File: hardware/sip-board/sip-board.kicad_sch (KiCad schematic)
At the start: 16 parts, among them Q5 BS170F

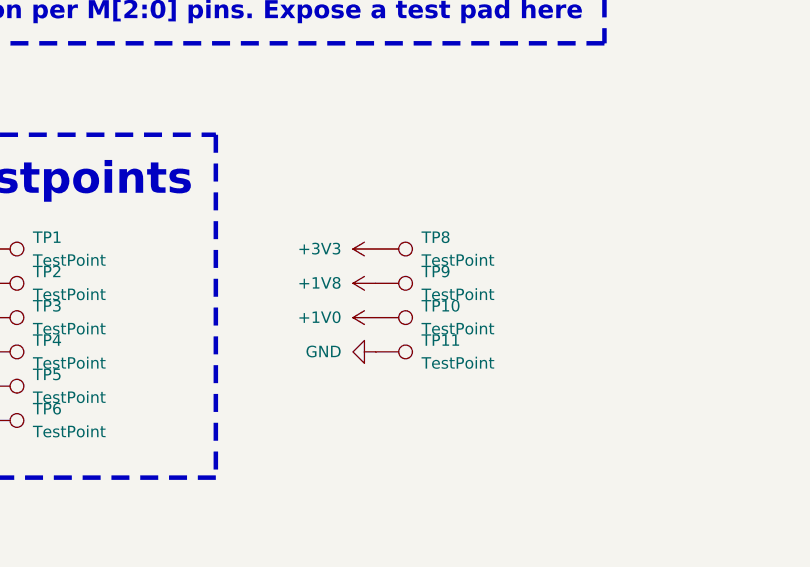
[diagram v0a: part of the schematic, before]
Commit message: sip vreg redo, connect level shifters to outside pins
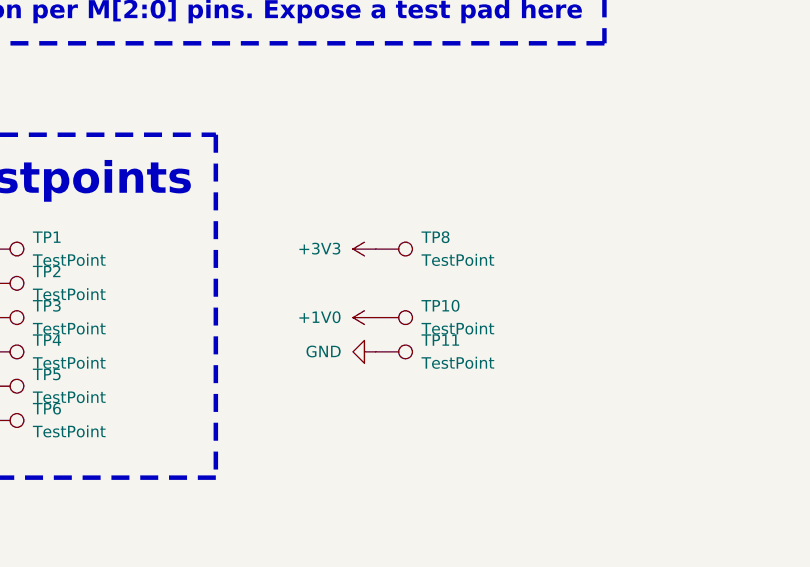
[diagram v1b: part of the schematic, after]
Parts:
- removed TP9: TestPoint, TestPoint:TestPoint_Pad_1.0x1.0mm, symbol Connector:TestPoint
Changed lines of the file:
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@@
-	(symbol
-		(lib_id "Connector:TestPoint")
-		(at 185.42 124.46 270)
-		(unit 1)
-		(exclude_from_sim no)
-		(in_bom yes)
-		(on_board yes)
-		(dnp no)
-		(fields_autoplaced yes)
-		(property "Reference" "TP9"
-			(at 190.5 123.1899 90)
-			(effects
-				(font
-					(size 1.27 1.27)
-				)
-				(justify left)
-			)
-		)
-		(property "Value" "TestPoint"
-			(at 190.5 125.7299 90)
-			(effects
-				(font
-					(size 1.27 1.27)
-				)
-				(justify left)
-			)
-		)
-		(property "Footprint" "TestPoint:TestPoint_Pad_1.0x1.0mm"
-			(at 185.42 129.54 0)
-			(effects
-				(font
-					(size 1.27 1.27)
-				)
-				(hide yes)
-			)
-		)
-		(property "Datasheet" "~"
-			(at 185.42 129.54 0)
-			(effects
-				(font
-					(size 1.27 1.27)
-				)
-				(hide yes)
-			)
-		)
-		(property "Description" "test point"
-			(at 185.42 124.46 0)
-			(effects
-				(font
-					(size 1.27 1.27)
-				)
-				(hide yes)
-			)
-		)
-		(pin "1"
-		)
-		(instances
-			(project "sip-board"
-				(path "/4eae758a-da4d-4448-84d4-770db7217b0d"
-					(reference "TP9")
-					(unit 1)
-				)
-			)
-		)
-	)
 	(symbol
 		(lib_id "Connector:TestPoint")
@@
 					(unit 1)
 				)
-			)
-		)
-	)
-	(symbol
-		(lib_id "power:+1V8")
-		(at 185.42 124.46 90)
-		(unit 1)
-		(exclude_from_sim no)
-		(in_bom yes)
-		(on_board yes)
-		(dnp no)
-		(fields_autoplaced yes)
-		(property "Reference" "#PWR0145"
-			(at 189.23 124.46 0)
-			(effects
-				(font
-					(size 1.27 1.27)
-				)
-				(hide yes)
-			)
-		)
-		(property "Value" "+1V8"
-			(at 181.61 124.4599 90)
-			(effects
-				(font
-					(size 1.27 1.27)
-				)
-				(justify left)
-			)
-		)
-		(property "Footprint" ""
-			(at 185.42 124.46 0)
-			(effects
-				(font
-					(size 1.27 1.27)
-				)
-				(hide yes)
-			)
-		)
-		(property "Datasheet" ""
-			(at 185.42 124.46 0)
-			(effects
-				(font
-					(size 1.27 1.27)
-				)
-				(hide yes)
-			)
-		)
-		(property "Description" "Power symbol creates a global label with name \"+1V8\""
-			(at 185.42 124.46 0)
-			(effects
-				(font
-					(size 1.27 1.27)
-				)
-				(hide yes)
-			)
-		)
-		(pin "1"
-		)
-		(instances
-			(project "sip-board"
-				(path "/4eae758a-da4d-4448-84d4-770db7217b0d"
-					(reference "#PWR0145")
-					(unit 1)
-				)
